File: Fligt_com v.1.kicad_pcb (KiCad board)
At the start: 2 copper layers, 9 parts, among them IC1 MS560702BA03-50, IC2 MMC5983MA, J1 Conn_01x04_Pin, J2 Conn_01x05_Pin

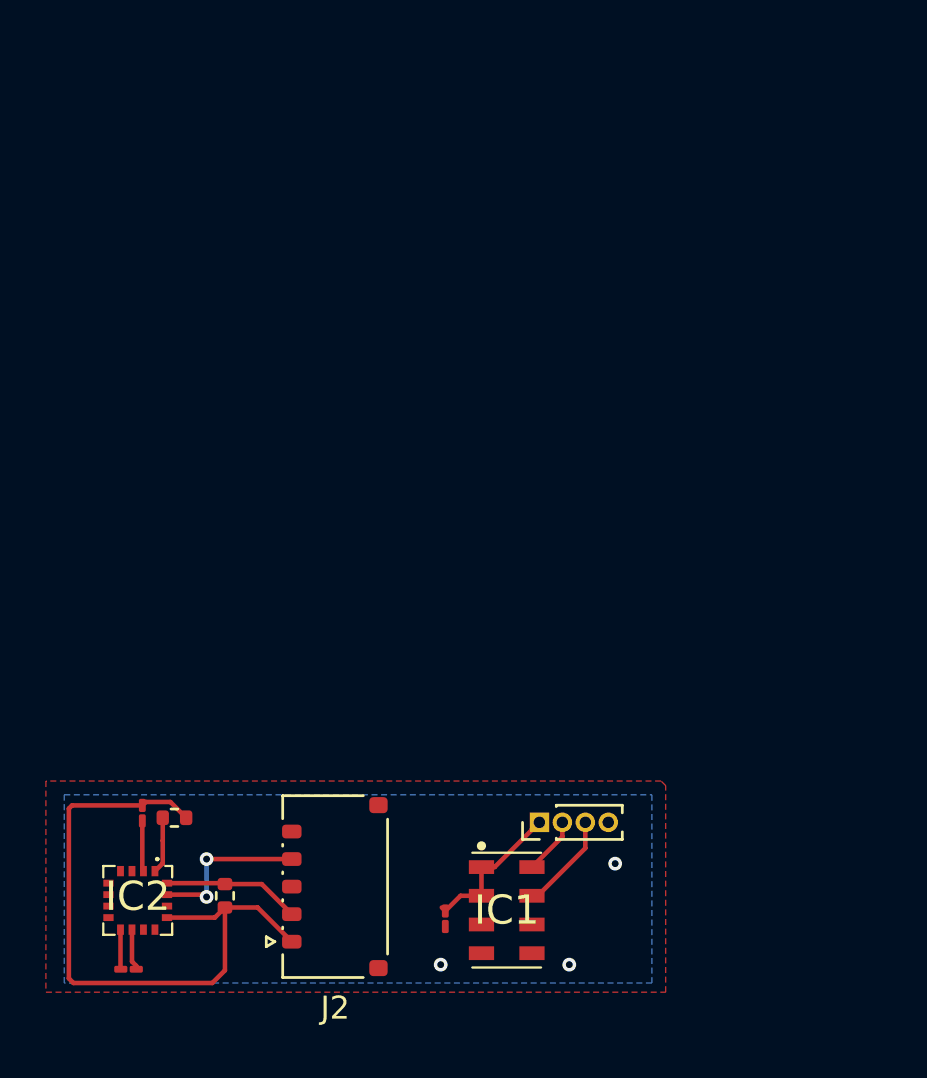
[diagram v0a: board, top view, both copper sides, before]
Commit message: Update avionics PCB schematic
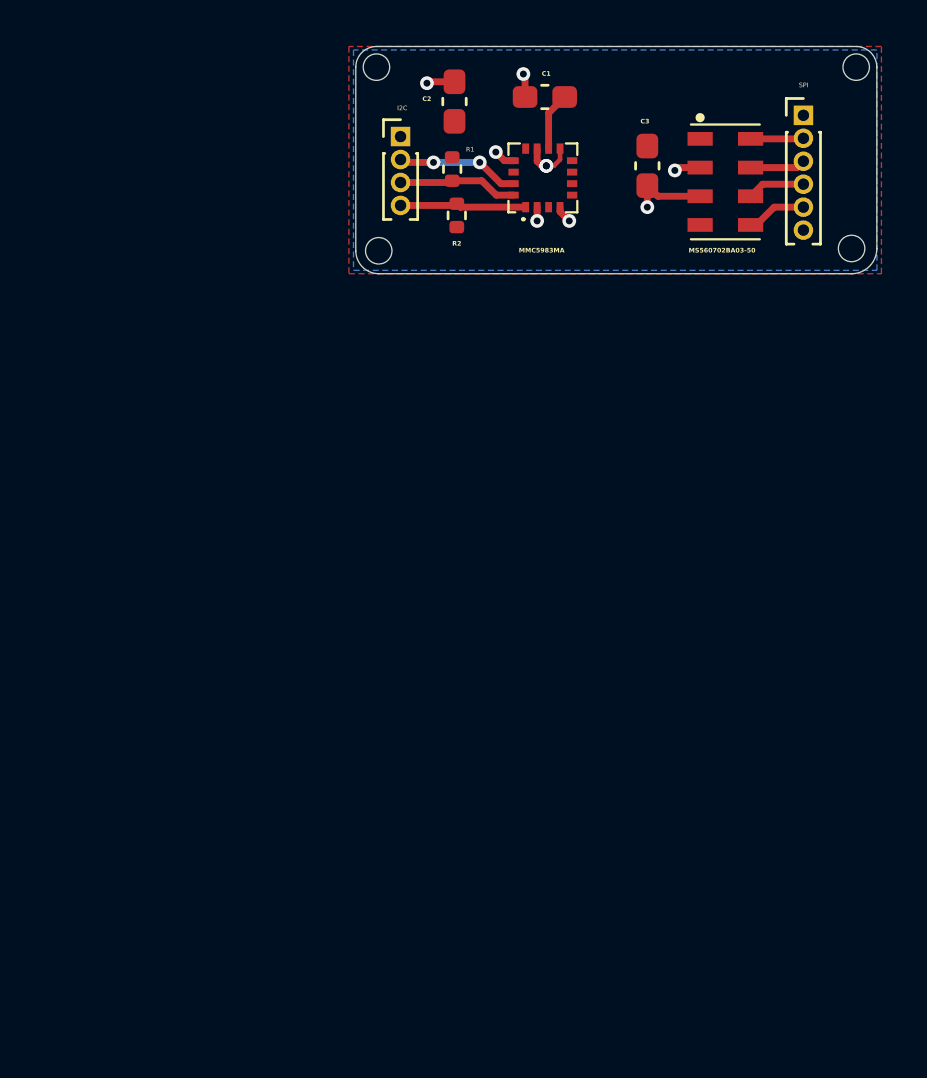
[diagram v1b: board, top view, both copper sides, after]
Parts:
- removed 2.7k1, 2.7k2: R, Resistor_SMD:R_0402_1005Metric
- added H1: MountingHole, MountingHole:ToolingHole_1.152mm, F.Cu at (145.2, 114.1)
- added H2: MountingHole, MountingHole:ToolingHole_1.152mm, F.Cu at (166.1, 114.1)
- added H3: MountingHole, MountingHole:ToolingHole_1.152mm, F.Cu at (165.9, 122.0)
- added H4: MountingHole, MountingHole:ToolingHole_1.152mm, F.Cu at (145.3, 122.1)
- added R1: 2.7k, Resistor_SMD:R_0402_1005Metric, F.Cu at (148.5, 118.5)
- added R2: 2.7k, Resistor_SMD:R_0402_1005Metric, F.Cu at (148.7, 120.6)
- 100n1, 10u1, 1u1: footprint Capacitor_SMD:C_01005_0402Metric_Pad0.57x0.30mm_HandSolder -> Capacitor_SMD:C_0603_1608Metric_Pad1.08x0.95mm_HandSolder
- J1: value Conn_01x04_Pin -> Conn_01x06_Pin; footprint Connector_PinHeader_1.00mm:PinHeader_1x04_P1.00mm_Vertical -> Connector_PinHeader_1.00mm:PinHeader_1x06_P1.00mm_Vertical
- J2: value Conn_01x05_Pin -> Conn_01x04_Pin; footprint Connector_Hirose:Hirose_DF57H-5P-1.2V_1x05_P1.2mm_Socket -> Connector_PinHeader_1.00mm:PinHeader_1x04_P1.00mm_Vertical
- moved 10u1 42.1 mm to (152.5, 115.4)
- moved IC2 36.1 mm to (152.4, 118.9), turned to 180 degrees
- moved 100n1 34.0 mm to (157.0, 118.4)
- moved 1u1 33.9 mm to (148.6, 115.6), turned to -90 degrees
- moved IC1 33.1 mm to (160.4, 119.1)
- moved J1 32.9 mm to (163.8, 116.2), turned to 0 degrees
- moved J2 32.8 mm to (146.2, 117.1), turned to 0 degrees
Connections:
- 1u1 pad 1: Net-(IC2-VDD) -> GND
- IC1 pad 2: +3.3V -> GND
- IC1 pad 4: GND -> unconnected-(IC1-CSB_1-Pad4)
- IC1 pad 5: GND -> MS5607_CS
- IC1 pad 6: unconnected-(IC1-SDO-Pad6) -> SDO
- IC2 pad 1: SCL -> SCK
- IC2 pad 2: Net-(IC2-VDD) -> +3.3V
- IC2 pad 4: unconnected-(IC2-SPI_CS-Pad4) -> +3.3V
- J1 pad 4: GND -> SDO
- J2 pad 1: +3.3V -> GND
- J2 pad 2: SDA -> INT
- J2 pad 3: SCL -> SDA
- J2 pad 4: INT -> SCK
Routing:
- net +3.3V: track 35.6 -> 2.30 mm, vias 0 -> 3
- net GND: track 1.73 -> 9.14 mm, vias 3 -> 6
- net SCK: track 0.00 -> 5.54 mm
- net MS5607_CS: track 0.00 -> 2.62 mm
- net SDO: track 0.00 -> 2.52 mm
- net SCL: track 2.47 -> 0.00 mm
- net Net-(IC2-VDD): track 2.21 -> 0.00 mm
- net SDI: track 4.31 -> 2.41 mm
- net INT: track 7.13 -> 5.36 mm
- net SDA: track 6.00 -> 5.21 mm
- net Net-(IC2-CAP): track 1.80 -> 2.54 mm
- added copper zone on F.Cu, net +3.3V
- added copper zone on B.Cu, net GND
- removed copper zone on B.Cu, net +3.3V
- removed copper zone on F.Cu, net GND
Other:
- board outline added: 22.7 x 9.9 mm
- board text added: "C1"
- board text added: "C2"
- board text added: "C3"
- board text added: "I2C"
- board text added: "MMC5983MA"
- board text added: "MS560702BA03-50"
- board text added: "R1"
- board text added: "R2"
- board text added: "SPI"
